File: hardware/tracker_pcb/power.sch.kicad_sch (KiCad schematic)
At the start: 21 parts, among them U3 TPS62933FDRLR, U4 TPS2117DRLR, U5 TLV1117LV33DCYR

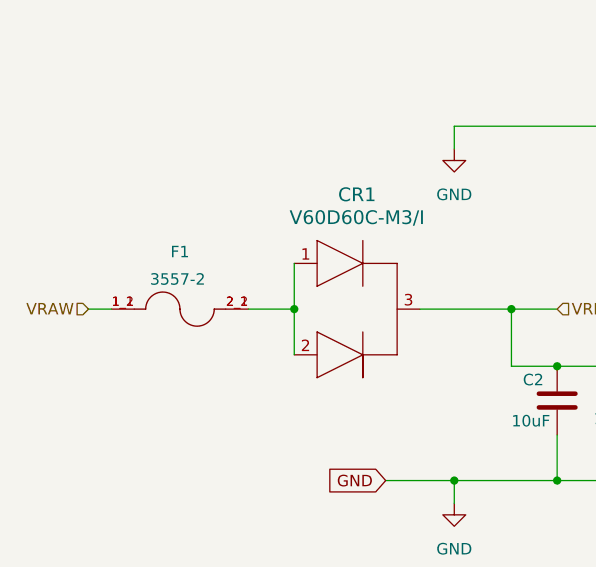
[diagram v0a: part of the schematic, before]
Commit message: Changed to phenix screw terminal connectors
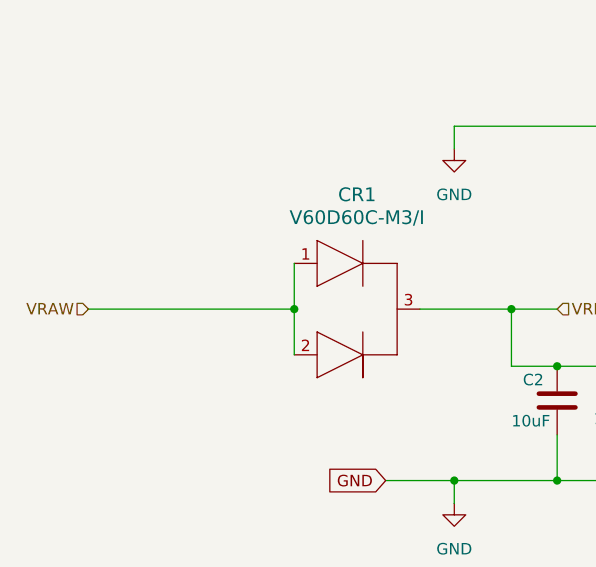
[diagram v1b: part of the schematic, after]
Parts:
- removed F1: 3557-2, footprint:FUSE_3557-2, symbol symbol:3557-2
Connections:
- net VRAW: now also CR1.1, CR1.2
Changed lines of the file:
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@@
 	(wire
 		(pts
-			(xy 49.53 87.63) (xy 52.07 87.63)
+			(xy 49.53 87.63) (xy 72.39 87.63)
 		)
 		(stroke
@@
 		(pts
 			(xy 215.9 46.99) (xy 204.47 46.99)
-		)
-		(stroke
-			(width 0)
-			(type default)
-		)
-	)
-	(wire
-		(pts
-			(xy 67.31 87.63) (xy 72.39 87.63)
 		)
 		(stroke
@@
 					(unit 1)
 				)
-			)
-		)
-	)
-	(symbol
-		(lib_id "symbol:3557-2")
-		(at 59.69 87.63 0)
-		(unit 1)
-		(exclude_from_sim no)
-		(in_bom yes)
-		(on_board yes)
-		(dnp no)
-		(property "Reference" "F1"
-			(at 59.69 81.28 0)
-			(effects
-				(font
-					(size 1.27 1.27)
-				)
-			)
-		)
-		(property "Value" "3557-2"
-			(at 59.436 84.328 0)
-			(effects
-				(font
-					(size 1.27 1.27)
-				)
-			)
-		)
-		(property "Footprint" "footprint:FUSE_3557-2"
-			(at 59.69 87.63 0)
-			(effects
-				(font
-					(size 1.27 1.27)
-				)
-				(justify bottom)
-				(hide yes)
-			)
-		)
-		(property "Datasheet" ""
-			(at 59.69 87.63 0)
-			(effects
-				(font
-					(size 1.27 1.27)
-				)
-				(hide yes)
-			)
-		)
-		(property "Description" ""
-			(at 59.69 87.63 0)
-			(effects
-				(font
-					(size 1.27 1.27)
-				)
-				(hide yes)
-			)
-		)
-		(property "PARTREV" "D"
-			(at 59.69 87.63 0)
-			(effects
-				(font
-					(size 1.27 1.27)
-				)
-				(justify bottom)
-				(hide yes)
-			)
-		)
-		(property "STANDARD" "Manufacturer Recommendation"
-			(at 59.69 87.63 0)
-			(effects
-				(font
-					(size 1.27 1.27)
-				)
-				(justify bottom)
-				(hide yes)
-			)
-		)
-		(property "SNAPEDA_PN" "3557-2"
-			(at 59.69 87.63 0)
-			(effects
-				(font
-					(size 1.27 1.27)
-				)
-				(justify bottom)
-				(hide yes)
-			)
-		)
-		(property "MAXIMUM_PACKAGE_HEIGHT" "7.37mm"
-			(at 59.69 87.63 0)
-			(effects
-				(font
-					(size 1.27 1.27)
-				)
-				(justify bottom)
-				(hide yes)
-			)
-		)
-		(property "MANUFACTURER" "Keystone"
-			(at 59.69 87.63 0)
-			(effects
-				(font
-					(size 1.27 1.27)
-				)
-				(justify bottom)
-				(hide yes)
-			)
-		)
-		(pin "1_2"
-		)
-		(pin "2_1"
-		)
-		(pin "1_1"
-		)
-		(pin "2_2"
-		)
-		(instances
-			(project ""
-				(path "/6aaa9514-f94e-4843-90d0-16960e4e49cb/4c324161-c4da-41f3-8af5-33f4b9a0442d"
-					(reference "F1")
-					(unit 1)
-				)

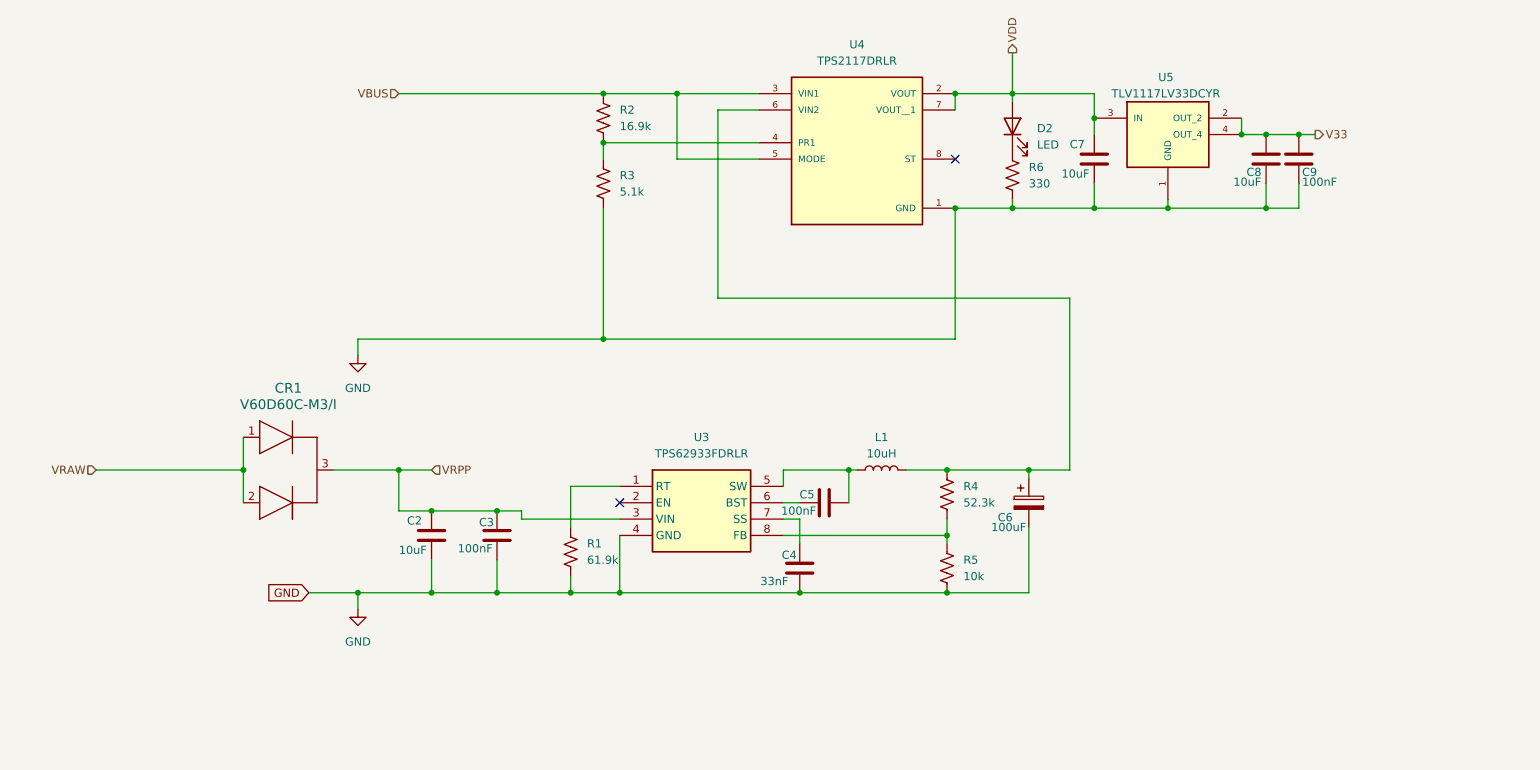
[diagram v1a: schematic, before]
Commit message: Beef up 5v supply and add new power mux
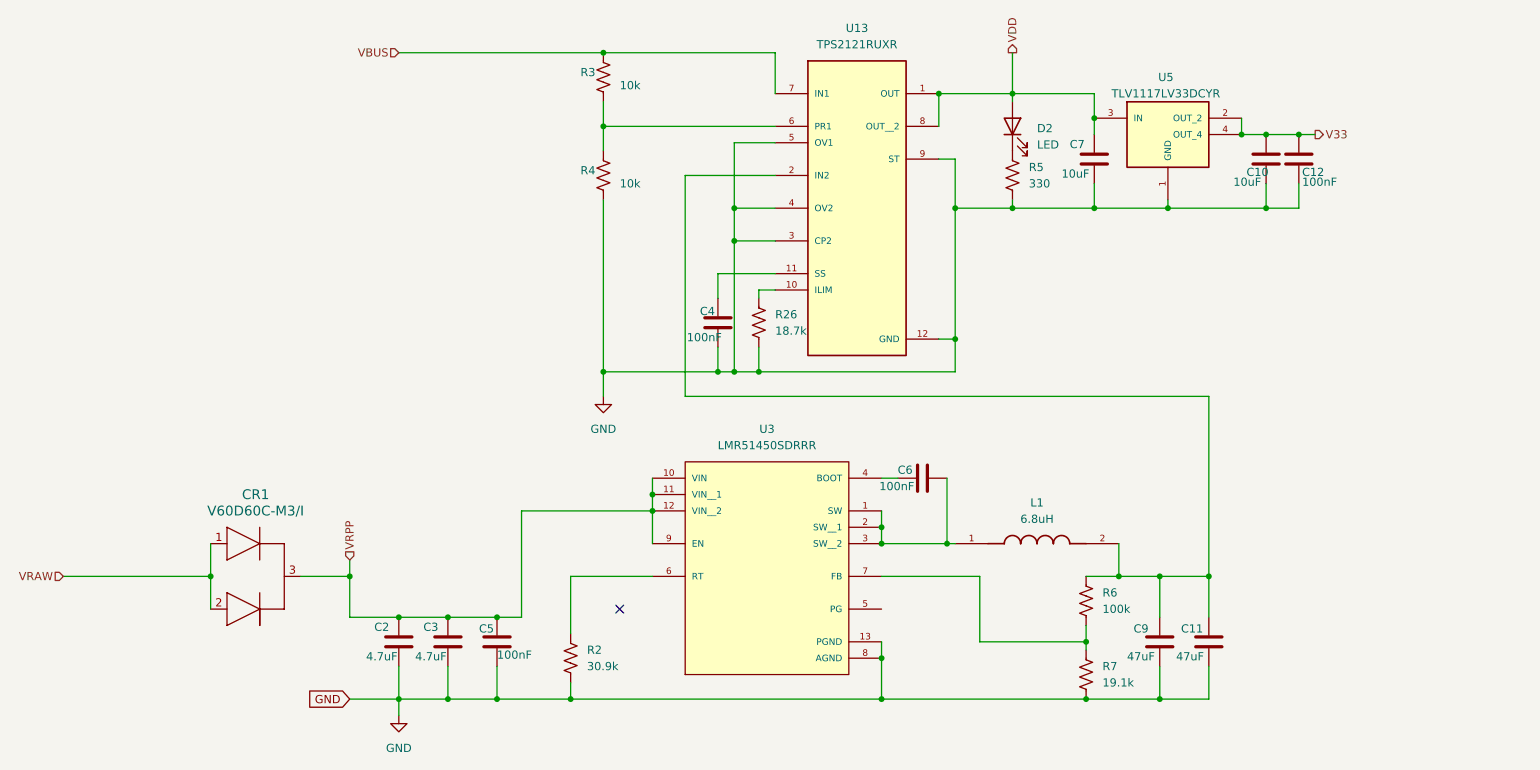
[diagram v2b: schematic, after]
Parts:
- removed C6: 100uF, Capacitor_SMD:CP_Elec_10x10.5, symbol Device:C_Polarized
- removed L1: 10uH, Inductor_SMD:L_Changjiang_FXL1350, symbol Device:L
- removed R3: 5.1k, Resistor_SMD:R_0603_1608Metric, symbol Device:R_US
- removed U3: TPS62933FDRLR, footprint:SOTFL50P160X60-8N, symbol symbol:TPS62933FDRLR
- removed U4: TPS2117DRLR, footprint:SOTFL50P160X60-8N, symbol symbol:TPS2117DRLR
- added C11, C9: 47uF, Capacitor_SMD:C_1210_3225Metric, symbol Device:C
- added C2: 4.7uF, Capacitor_SMD:C_1206_3216Metric, symbol Device:C
- added L1: 6.8uH, footprint:IND_XAL6060-682MEC, symbol symbol:XAL6060-682MEC
- added R26: 18.7k, Resistor_SMD:R_0402_1005Metric, symbol Device:R_US
- added R4: 10k, Resistor_SMD:R_0402_1005Metric, symbol Device:R_US
- added U13: TPS2121RUXR, footprint:IC_TPS2121RUXR, symbol symbol:TPS2121RUXR
- added U3: LMR51450SDRRR, footprint:CONV_LMR51450SDRRR, symbol symbol:LMR51450SDRRR
- C3: renamed from C2; value 10uF -> 4.7uF; LCSC C1849 -> C77096
- C4: value 33nF -> 100nF; footprint Capacitor_SMD:C_0603_1608Metric -> Capacitor_SMD:C_0402_1005Metric; LCSC C1614 -> C1525
- R2: renamed from R1; value 61.9k -> 30.9k; LCSC C23091 -> C137744
- R3: renamed from R2; value 16.9k -> 10k; footprint Resistor_SMD:R_0603_1608Metric -> Resistor_SMD:R_0402_1005Metric; LCSC C25954 -> C25744
- R6: renamed from R4; value 52.3k -> 100k; LCSC C185323 -> C844916
- R7: renamed from R5; value 10k -> 19.1k; LCSC C25804 -> C844132
- renumbered C8 to C10, C9 to C12, C3 to C5, C5 to C6, R6 to R5
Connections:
- net GND: now also C11.2, C2.2, C9.2, R26.1, R4.1, U13.12 (GND), U13.3 (CP2), U13.4 (OV2), U13.5 (OV1), U13.9 (ST), U3.13 (PGND), U3.8 (AGND)
- net VBUS: now also U13.7 (IN1)
- net VDD: now also U13.1 (OUT), U13.8 (OUT__2)
- net VRPP: now also C2.1, U3.10 (VIN), U3.11 (VIN__1), U3.12 (VIN__2), U3.9 (EN)
- net at C6.1: now also U3.4 (BOOT)
- net at C6.2: now also L1.1, U3.1 (SW), U3.2 (SW__1), U3.3 (SW__2)
- net at R2.2: now also U3.6 (RT)
- net at C4.1: now also U13.11 (SS)
- net at R6.1, R7.2: now also U3.7 (FB)
- net at R3.1: now also R4.2, U13.6 (PR1)
- net at R6.2: now also C11.1, C9.1, L1.2, U13.2 (IN2)
- new net: R26.2, U13.10 (ILIM)
- no-connect marks 2 -> 1
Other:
- moved on the sheet: C3, C5, C6, CR1, R2, R3, R6, R7

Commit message: Modify iso circuit for best CTR
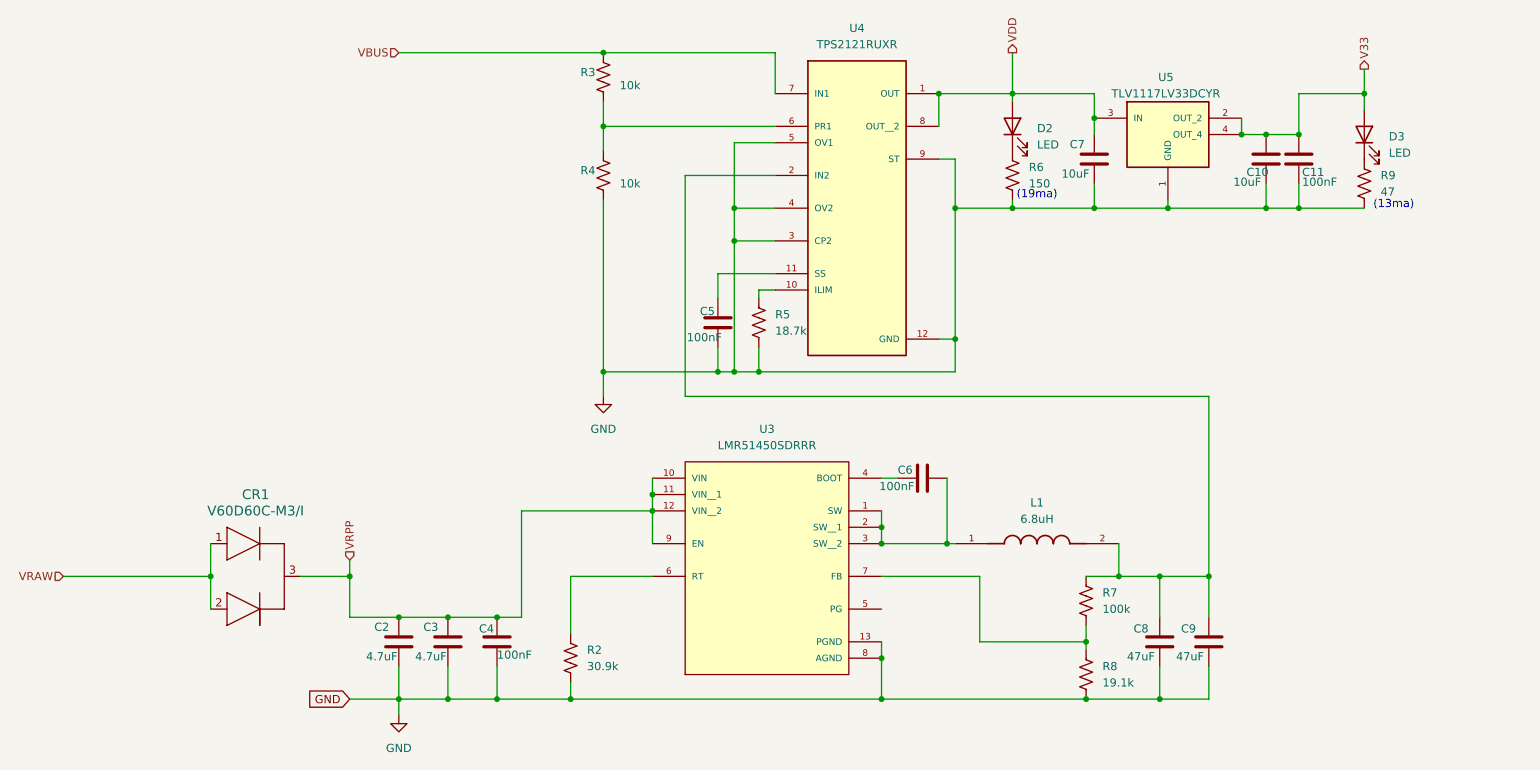
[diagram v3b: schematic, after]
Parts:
- added D3: LED, LED_SMD:LED_0603_1608Metric, symbol Device:LED
- added R9: 47, Resistor_SMD:R_0603_1608Metric, symbol Device:R_US
- R6: renamed from R5; value 330 -> 150; LCSC C23138 -> C22808
- renumbered C12 to C11, C5 to C4, C4 to C5, C9 to C8, C11 to C9, R26 to R5, R6 to R7, R7 to R8, U13 to U4
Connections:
- net GND: now also R9.1
- net V33: now also D3.2 (A)
- new net: D3.1 (K), R9.2
- no-connect marks 1 -> 0
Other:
- note added: "(13ma)"
- note added: "(19ma)"

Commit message: update BOM
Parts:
- R2: LCSC C137744 -> C23022
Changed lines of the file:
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@@
 			)
 		)
-		(property "LCSC" "C137744"
+		(property "LCSC" "C23022"
 			(at 125.73 115.5699 0)
 			(effects

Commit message: v2 hardware changes
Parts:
- renumbered C9 to C10, C10 to C11, C11 to C12, C2 to C3, C3 to C4, C4 to C5, C5 to C6, C6 to C7, C7 to C8, C8 to C9, R8 to R10, R9 to R11, R2 to R4, R3 to R5, R4 to R6, R5 to R7, R6 to R8, R7 to R9
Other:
- note added: "Change to 150R"
- note added: "Change to 470R"
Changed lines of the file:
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@@
 	(generator_version "9.0")
 	(paper "A4")
+	(text "Change to 470R"
+		(exclude_from_sim no)
+		(at 197.866 49.784 0)
+		(effects
+			(font
+				(size 1.27 1.27)
+			)
+		)
+	)
 	(text "(13ma)"
 		(exclude_from_sim no)
@@
 		)
 	)
+	(text "Change to 150R"
+		(exclude_from_sim no)
+		(at 262.636 45.212 0)
+		(effects
+			(font
+				(size 1.27 1.27)
+			)
+		)
+	)
 	(junction
 		(at 128.27 34.29)
@@
 		(on_board yes)
 		(dnp no)
-		(property "Reference" "C2"
+		(property "Reference" "C3"
 			(at 92.71 112.014 0)
 			(effects
@@
 			(project "tracker_pcb"
 				(path "/6aaa9514-f94e-4843-90d0-16960e4e49cb/4c324161-c4da-41f3-8af5-33f4b9a0442d"
-					(reference "C2")
+					(reference "C3")
 					(unit 1)
 				)
@@
 		(dnp no)
 		(fields_autoplaced yes)
-		(property "Reference" "R6"
+		(property "Reference" "R8"
 			(at 194.31 40.6399 0)
 			(effects
@@
 			(project "tracker_pcb"
 				(path "/6aaa9514-f94e-4843-90d0-16960e4e49cb/4c324161-c4da-41f3-8af5-33f4b9a0442d"
-					(reference "R6")
+					(reference "R8")
 					(unit 1)
 				)
@@
 		(on_board yes)
 		(dnp no)
-		(property "Reference" "C4"
+		(property "Reference" "C5"
 			(at 108.966 112.268 0)
 			(effects
@@
 			(project "tracker_pcb"
 				(path "/6aaa9514-f94e-4843-90d0-16960e4e49cb/4c324161-c4da-41f3-8af5-33f4b9a0442d"
-					(reference "C4")
+					(reference "C5")
 					(unit 1)
 				)
@@
 		(on_board yes)
 		(dnp no)
-		(property "Reference" "C6"
+		(property "Reference" "C7"
 			(at 176.276 87.63 90)
 			(effects
@@
 			(project "tracker_pcb"
 				(path "/6aaa9514-f94e-4843-90d0-16960e4e49cb/4c324161-c4da-41f3-8af5-33f4b9a0442d"
-					(reference "C6")
+					(reference "C7")
 					(unit 1)
 				)
@@
 		(dnp no)
 		(fields_autoplaced yes)
-		(property "Reference" "#PWR012"
+		(property "Reference" "#PWR013"
 			(at 96.52 132.08 0)
 			(effects
@@
 			(project "tracker_pcb"
 				(path "/6aaa9514-f94e-4843-90d0-16960e4e49cb/4c324161-c4da-41f3-8af5-33f4b9a0442d"
-					(reference "#PWR012")
+					(reference "#PWR013")
 					(unit 1)
 				)
@@
 		(on_board yes)
 		(dnp no)
-		(property "Reference" "R4"
+		(property "Reference" "R6"
 			(at 124.714 41.148 0)
 			(effects
@@
 			(project "tracker_pcb"
 				(path "/6aaa9514-f94e-4843-90d0-16960e4e49cb/4c324161-c4da-41f3-8af5-33f4b9a0442d"
-					(reference "R4")
+					(reference "R6")
 					(unit 1)
 				)
@@
 		(dnp no)
 		(fields_autoplaced yes)
-		(property "Reference" "R2"
+		(property "Reference" "R4"
 			(at 125.73 115.5699 0)
 			(effects
@@
 			(project "tracker_pcb"
 				(path "/6aaa9514-f94e-4843-90d0-16960e4e49cb/4c324161-c4da-41f3-8af5-33f4b9a0442d"
-					(reference "R2")
+					(reference "R4")
 					(unit 1)
 				)
@@
 		(on_board yes)
 		(dnp no)
-		(property "Reference" "C10"
+		(property "Reference" "C11"
 			(at 228.092 41.402 0)
 			(effects
@@
 			(project "tracker_pcb"
 				(path "/6aaa9514-f94e-4843-90d0-16960e4e49cb/4c324161-c4da-41f3-8af5-33f4b9a0442d"
-					(reference "C10")
+					(reference "C11")
 					(unit 1)
 				)
@@
 		(on_board yes)
 		(dnp no)
-		(property "Reference" "C3"
+		(property "Reference" "C4"
 			(at 100.33 112.014 0)
 			(effects
@@
 			(project "tracker_pcb"
 				(path "/6aaa9514-f94e-4843-90d0-16960e4e49cb/4c324161-c4da-41f3-8af5-33f4b9a0442d"
-					(reference "C3")
+					(reference "C4")
 					(unit 1)
 				)
@@
 		(on_board yes)
 		(dnp no)
-		(property "Reference" "R3"
+		(property "Reference" "R5"
 			(at 124.714 25.908 0)
 			(effects
@@
 			(project "tracker_pcb"
 				(path "/6aaa9514-f94e-4843-90d0-16960e4e49cb/4c324161-c4da-41f3-8af5-33f4b9a0442d"
-					(reference "R3")
+					(reference "R5")
 					(unit 1)
 				)
@@
 		(on_board yes)
 		(dnp no)
-		(property "Reference" "C7"
+		(property "Reference" "C8"
 			(at 200.66 37.084 0)
 			(effects
@@
 			(project "tracker_pcb"
 				(path "/6aaa9514-f94e-4843-90d0-16960e4e49cb/4c324161-c4da-41f3-8af5-33f4b9a0442d"
-					(reference "C7")
+					(reference "C8")
 					(unit 1)
 				)
@@
 		(on_board yes)
 		(dnp no)
-		(property "Reference" "C9"
+		(property "Reference" "C10"
 			(at 217.932 112.268 0)
 			(effects
@@
 			(project "tracker_pcb"
 				(path "/6aaa9514-f94e-4843-90d0-16960e4e49cb/4c324161-c4da-41f3-8af5-33f4b9a0442d"
-					(reference "C9")
+					(reference "C10")
 					(unit 1)
 				)
@@
 		(dnp no)
 		(fields_autoplaced yes)
-		(property "Reference" "#PWR013"
+		(property "Reference" "#PWR014"
 			(at 128.27 82.55 0)
 			(effects
@@
 			(project "tracker_pcb"
 				(path "/6aaa9514-f94e-4843-90d0-16960e4e49cb/4c324161-c4da-41f3-8af5-33f4b9a0442d"
-					(reference "#PWR013")
+					(reference "#PWR014")
 					(unit 1)
 				)
@@
 		(on_board yes)
 		(dnp no)
-		(property "Reference" "C8"
+		(property "Reference" "C9"
 			(at 210.566 112.268 0)
 			(effects
@@
 			(project "tracker_pcb"
 				(path "/6aaa9514-f94e-4843-90d0-16960e4e49cb/4c324161-c4da-41f3-8af5-33f4b9a0442d"
-					(reference "C8")
+					(reference "C9")
 					(unit 1)
 				)
@@
 		(dnp no)
 		(fields_autoplaced yes)
-		(property "Reference" "R7"
+		(property "Reference" "R9"
 			(at 205.74 106.6799 0)
 			(effects
@@
 			(project "tracker_pcb"
 				(path "/6aaa9514-f94e-4843-90d0-16960e4e49cb/4c324161-c4da-41f3-8af5-33f4b9a0442d"
-					(reference "R7")
+					(reference "R9")
 					(unit 1)
 				)
@@
 		(dnp no)
 		(fields_autoplaced yes)
-		(property "Reference" "R5"
+		(property "Reference" "R7"
 			(at 154.94 63.4999 0)
 			(effects
@@
 			(project "tracker_pcb"
 				(path "/6aaa9514-f94e-4843-90d0-16960e4e49cb/4c324161-c4da-41f3-8af5-33f4b9a0442d"
-					(reference "R5")
+					(reference "R7")
 					(unit 1)
 				)
@@
 		(on_board yes)
 		(dnp no)
-		(property "Reference" "C5"
+		(property "Reference" "C6"
 			(at 143.256 62.992 0)
 			(effects
@@
 			(project "tracker_pcb"
 				(path "/6aaa9514-f94e-4843-90d0-16960e4e49cb/4c324161-c4da-41f3-8af5-33f4b9a0442d"
-					(reference "C5")
+					(reference "C6")
 					(unit 1)
 				)
@@
 		(on_board yes)
 		(dnp no)
-		(property "Reference" "C11"
+		(property "Reference" "C12"
 			(at 236.728 41.402 0)
 			(effects
@@
 			(project "tracker_pcb"
 				(path "/6aaa9514-f94e-4843-90d0-16960e4e49cb/4c324161-c4da-41f3-8af5-33f4b9a0442d"
-					(reference "C11")
+					(reference "C12")
 					(unit 1)
 				)
@@
 		(dnp no)
 		(fields_autoplaced yes)
-		(property "Reference" "R8"
+		(property "Reference" "R10"
 			(at 205.74 118.1099 0)
 			(effects
@@
 			(project "tracker_pcb"
 				(path "/6aaa9514-f94e-4843-90d0-16960e4e49cb/4c324161-c4da-41f3-8af5-33f4b9a0442d"
-					(reference "R8")
+					(reference "R10")
 					(unit 1)
 				)
@@
 		(dnp no)
 		(fields_autoplaced yes)
-		(property "Reference" "R9"
+		(property "Reference" "R11"
 			(at 248.92 41.9099 0)
 			(effects
@@
 			(project "tracker_pcb"
 				(path "/6aaa9514-f94e-4843-90d0-16960e4e49cb/4c324161-c4da-41f3-8af5-33f4b9a0442d"
-					(reference "R9")
+					(reference "R11")
 					(unit 1)
 				)
